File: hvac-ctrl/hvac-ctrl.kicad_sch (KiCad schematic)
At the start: 13 parts, among them J1 Screw_Terminal_01x03, J2 Screw_Terminal_01x02, J3 Screw_Terminal_01x03, J4 Screw_Terminal_01x02, U1 Module_LM2596_ADJ, U2 Module_LM2596_ADJ, U3 LD1117AV33

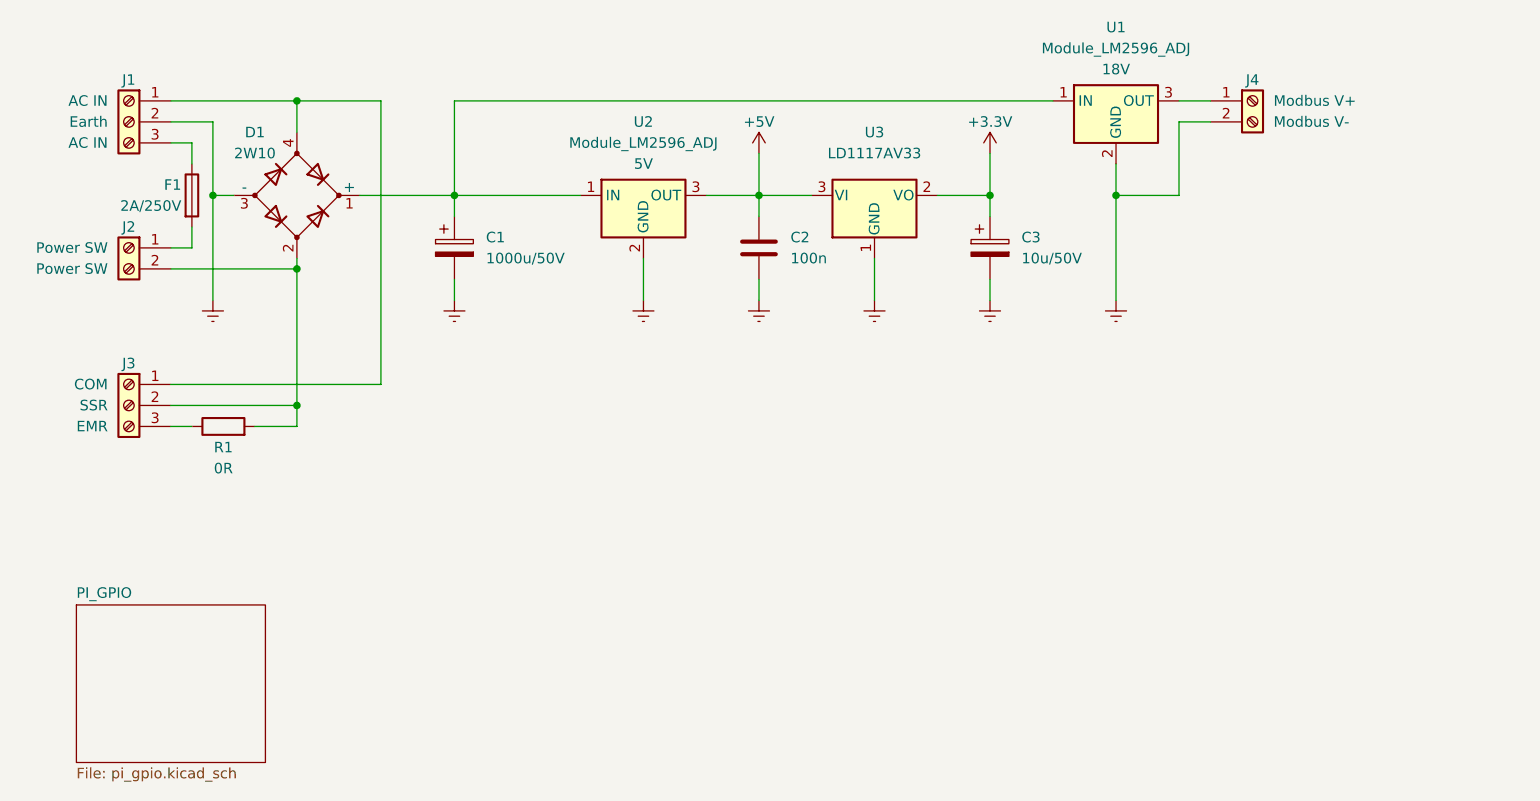
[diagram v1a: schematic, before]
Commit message: Update schematic with the latest prototype improvements
- Change series resistor value on the ERV control optocoupler LED side
- Add ERV power monitor LED.
- Add resistive dividers for sensing the 5V and 18V rails voltage.
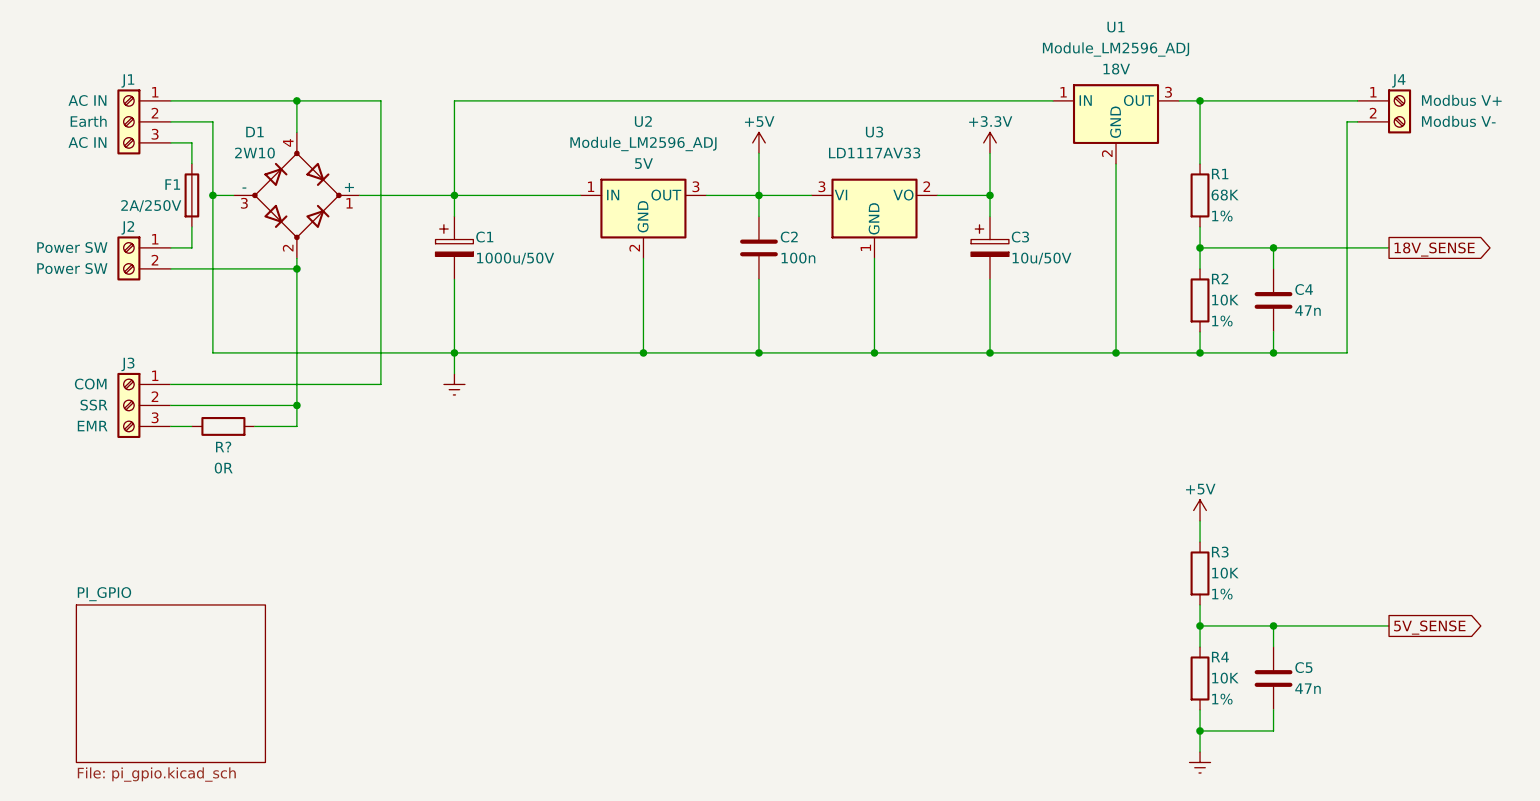
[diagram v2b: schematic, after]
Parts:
- added C4, C5: 47n, symbol Device:C
- added R1: 68K, symbol Device:R
- added R2, R3, R4: 10K, symbol Device:R
- renumbered R1 to R?
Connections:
- net +5V: now also R3.1
- net Earth: now also C4.2, C5.2, R2.2, R4.2
- net at J4.1 (Pin_1), U1.3 (OUT): now also R1.1
- new net 18V_SENSE: C4.1, R1.2, R2.1
- new net 5V_SENSE: C5.1, R3.2, R4.1
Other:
- moved on the sheet: J4
